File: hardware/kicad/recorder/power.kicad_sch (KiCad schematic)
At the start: 16 parts, among them U3 MCP73831-2-OT, U4 AP2112K-3.3, U5 AP22804AW5, U8 LP5907MFX-3.3

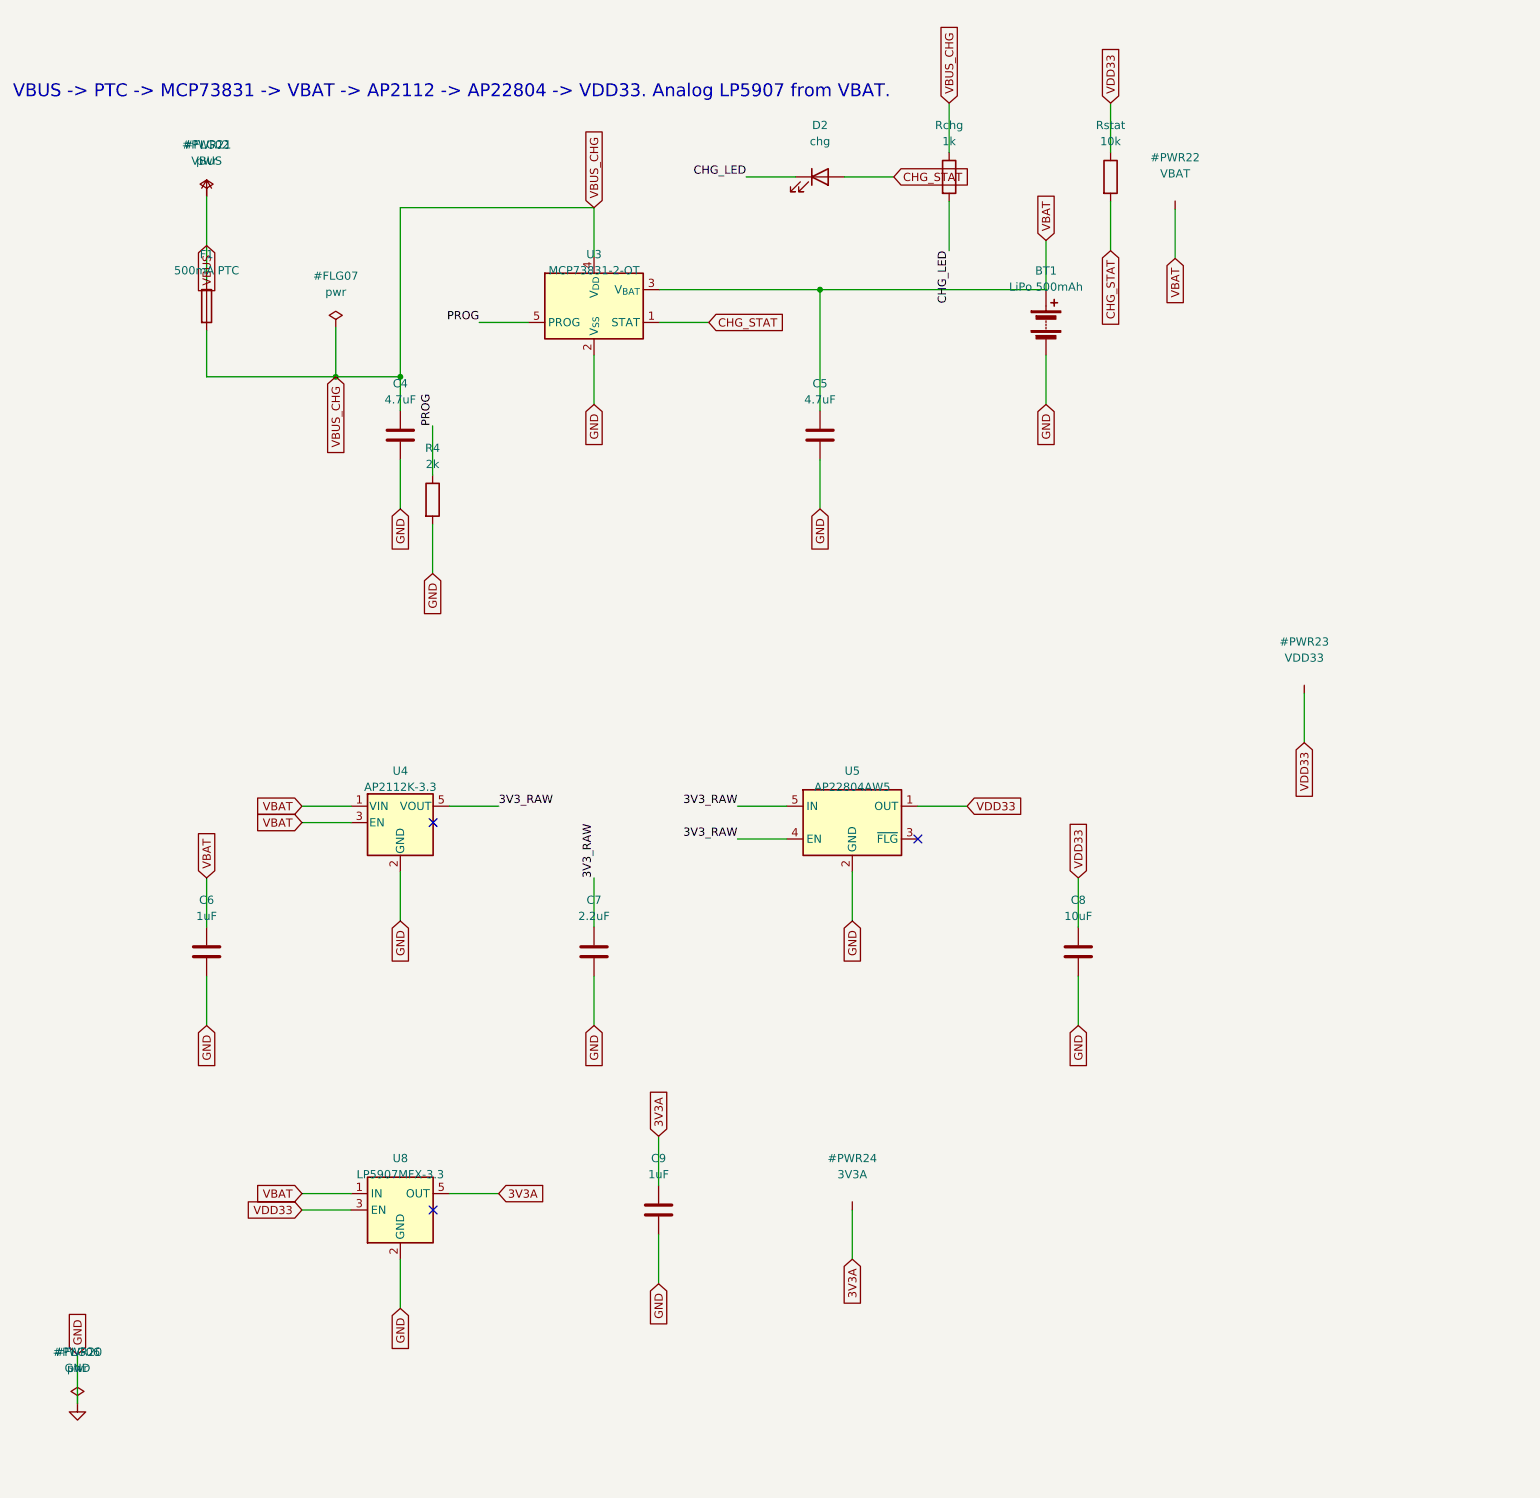
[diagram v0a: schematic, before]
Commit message: Swap in a BQ24074 power-path charger so USB can run the board with the pouch unplugged.
Co-authored-by: Cursor <cursoragent@cursor.com>
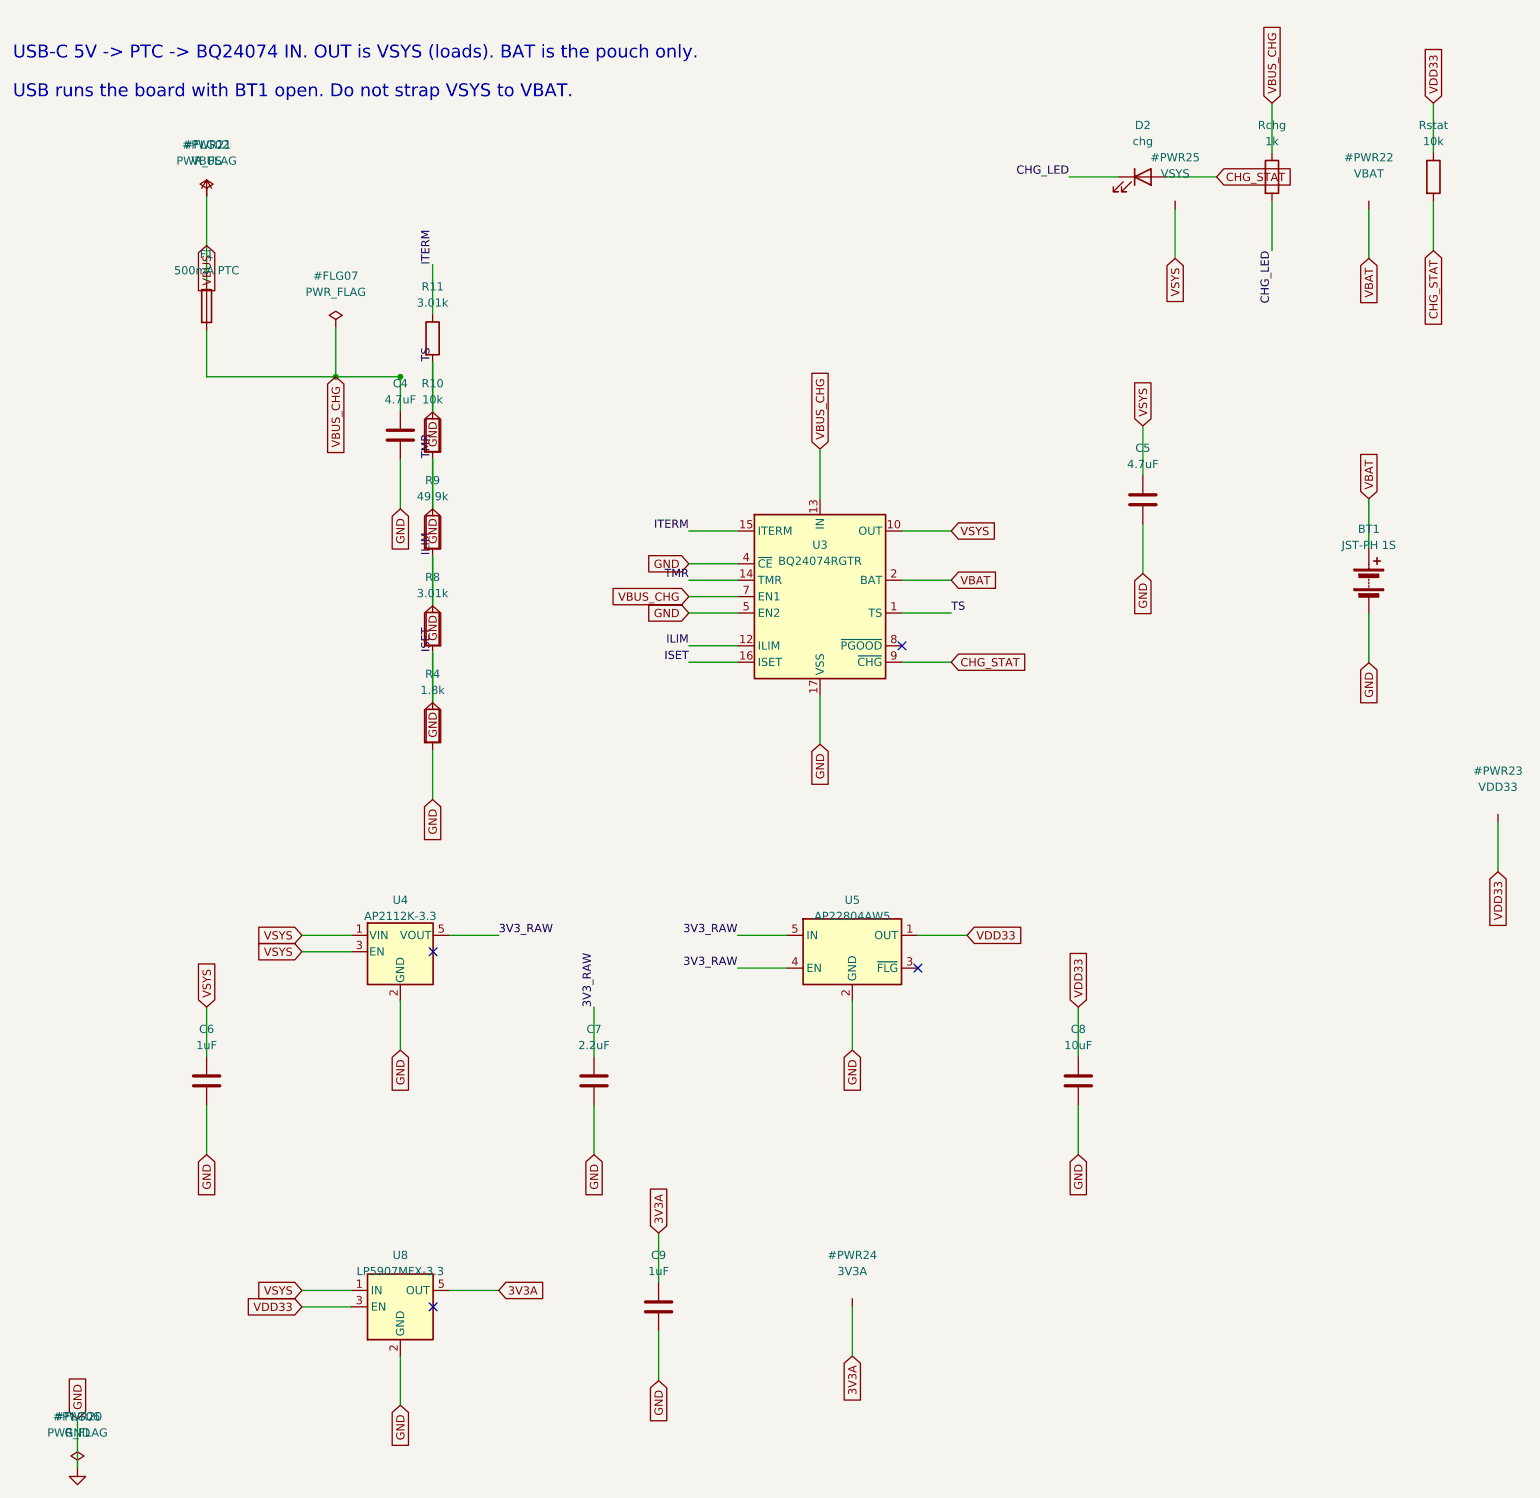
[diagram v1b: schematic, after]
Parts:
- added R10: 10k, Resistor_SMD:R_0603_1608Metric, symbol Device:R
- added R11, R8: 3.01k, Resistor_SMD:R_0603_1608Metric, symbol Device:R
- added R9: 49.9k, Resistor_SMD:R_0603_1608Metric, symbol Device:R
- BT1: value LiPo 500mAh -> JST-PH 1S; footprint Connector_Wire:SolderWire-2sqmm_1x02_P7.8mm_D2mm_OD3.9mm -> Connector_JST:JST_PH_S2B-PH-K_1x02_P2.00mm_Horizontal
- R4: value 2k -> 1.8k
- U3: value MCP73831-2-OT -> BQ24074RGTR; footprint Package_TO_SOT_SMD:SOT-23-5 -> Package_DFN_QFN:VQFN-16-1EP_3x3mm_P0.5mm_EP1.6x1.6mm; symbol Battery_Management:MCP73831-2-OT -> PSV:BQ24074RGT
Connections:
- net PROG is gone; now on net GND: R4.1, U3.5 (EN2)
- net CHG_STAT: now also U3.9 (~{CHG}); no longer U3.1 (STAT)
- net GND: now also U3.1 (TS), U3.12 (ILIM), U3.14 (TMR), U3.16 (ISET), U3.17 (VSS), U3.4 (~{CE}), R10.1, R10.2, R11.2, R8.1, R8.2, R9.1, R9.2; no longer U3.2 (V_{SS})
- net VBAT: now also U3.2 (BAT); no longer C5.1, C6.1, U4.1 (VIN), U4.3 (EN), U8.1 (IN)
- net VBUS_CHG renamed IN
- net IN: now also U3.13 (IN), U3.6 (IN), U3.7 (EN1); no longer U3.4 (V_{DD})
- new net ITERM: R11.1, U3.15 (ITERM)
- new net VSYS: C5.1, C6.1, U3.10 (OUT), U3.11 (OUT), U4.1 (VIN), U4.3 (EN), U8.1 (IN)
- no-connect marks 3 -> 4
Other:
- note added: "USB runs the board with BT1 open. Do not strap VSYS to VBAT."
- note added: "USB-C 5V -> PTC -> BQ24074 IN. OUT is VSYS (loads). BAT is the pouch only."
- note removed: "VBUS -> PTC -> MCP73831 -> VBAT -> AP2112 -> AP22804 -> VDD33. Analog LP5907 from VBAT."
- moved on the sheet: BT1, C5, C6, C7, C8, C9, D2, R4, Rchg, Rstat, U4, U5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

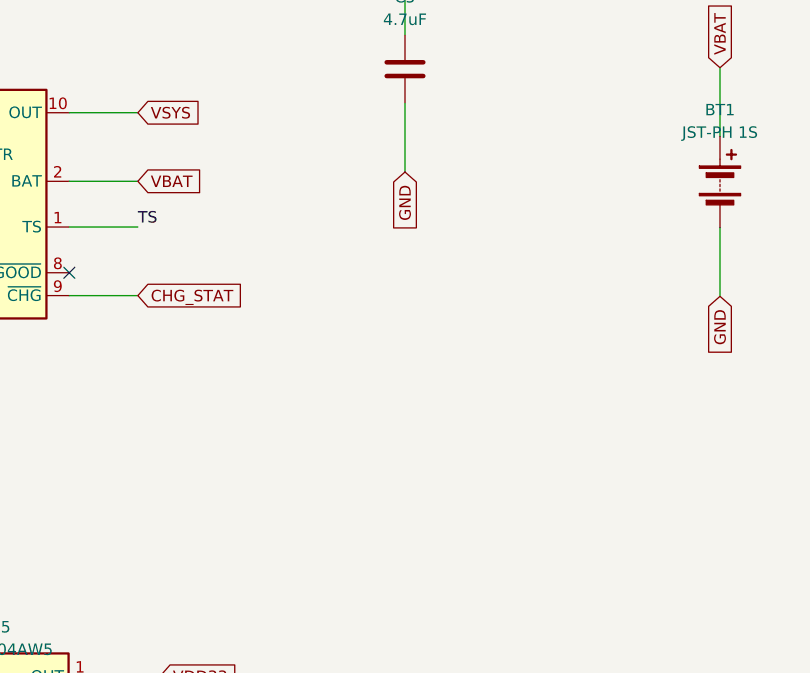
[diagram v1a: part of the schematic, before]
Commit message: Put the real JST-PH on BT1, add a BAT ceramic at U3, and document lid-off Boot/Reset.
The power-path PR still shipped a 7.8 mm solder-wire land while the BOM
named S2B-PH-K-S. Owner chose the real 2.00 mm connector: pad 1 stays at
(-23.5, 34) on VBAT so the existing B.Cu hop still hits it, pad 2 moves
to (-21.5, 34) on GND. C21 is 10 µF next to U3 BAT for USB with the pouch
unplugged. The 6.0 mm housing does not fit the 5.45 mm lid cavity, so the
case cuts a window through shell_back. Boot and Reset stay lid-off; a
flush hole would not reach the 5 mm actuators. power_path.cir now runs
USB-with-BT1-open and pouch-only through a BATFET.

Co-authored-by: Cursor <cursoragent@cursor.com>
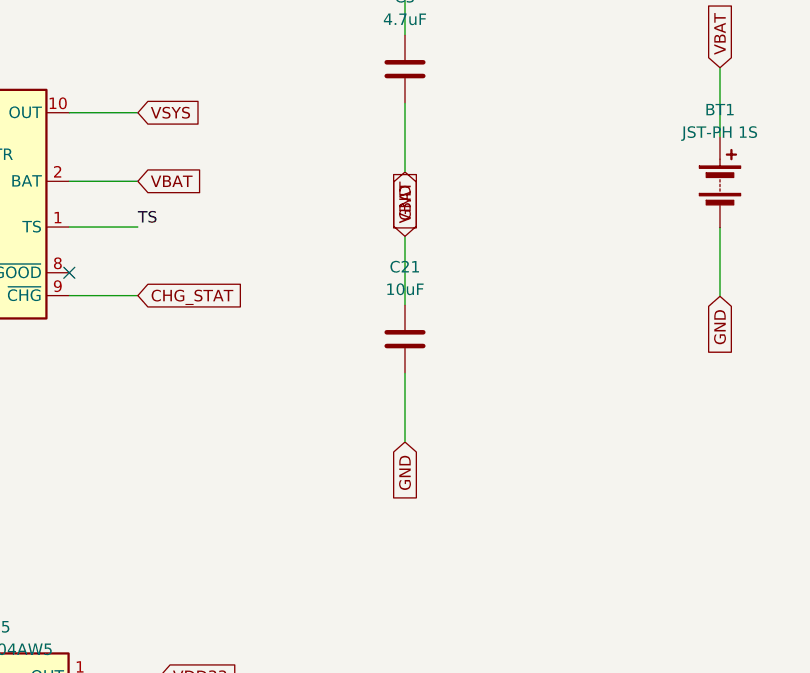
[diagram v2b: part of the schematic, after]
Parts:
- added C21: 10uF, Capacitor_SMD:C_0603_1608Metric, symbol Device:C
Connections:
- net GND: now also C21.2
- net VBAT: now also C21.1
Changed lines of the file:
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@@
+		(effects (font (size 1.27 1.27)) (justify right))
+	)
+	(symbol
+		(lib_id "Device:C")
+		(at 195.00 110.00 0)
+		(unit 1)
+		(exclude_from_sim no)
+		(in_bom yes)
+		(on_board yes)
+		(dnp no)
+		(property "Reference" "C21" (at 195.00 102.00 0)
+			(effects (font (size 1.27 1.27))))
+		(property "Value" "10uF" (at 195.00 104.50 0)
+			(effects (font (size 1.27 1.27))))
+		(property "Footprint" "Capacitor_SMD:C_0603_1608Metric" (at 195.00 110.00 0)
+			(effects (font (size 1.27 1.27)) hide))
+		(property "Datasheet" "~" (at 195.00 110.00 0)
+			(effects (font (size 1.27 1.27)) hide))
+		(pin "1")
+		(pin "2")
+	)
+	(wire
+		(pts (xy 195.00 106.19) (xy 195.00 98.57))
+		(stroke (width 0) (type default))
+	)
+	(global_label "VBAT"
+		(shape input)
+		(at 195.00 98.57 90)
+		(effects (font (size 1.27 1.27)) (justify left))
+	)
+	(wire
+		(pts (xy 195.00 113.81) (xy 195.00 121.43))
+		(stroke (width 0) (type default))
+	)
+	(global_label "GND"
+		(shape input)
+		(at 195.00 121.43 270)
 		(effects (font (size 1.27 1.27)) (justify right))
 	)
